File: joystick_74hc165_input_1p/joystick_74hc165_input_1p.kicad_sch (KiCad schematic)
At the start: 11 parts, among them J1 Conn_01x18_Male

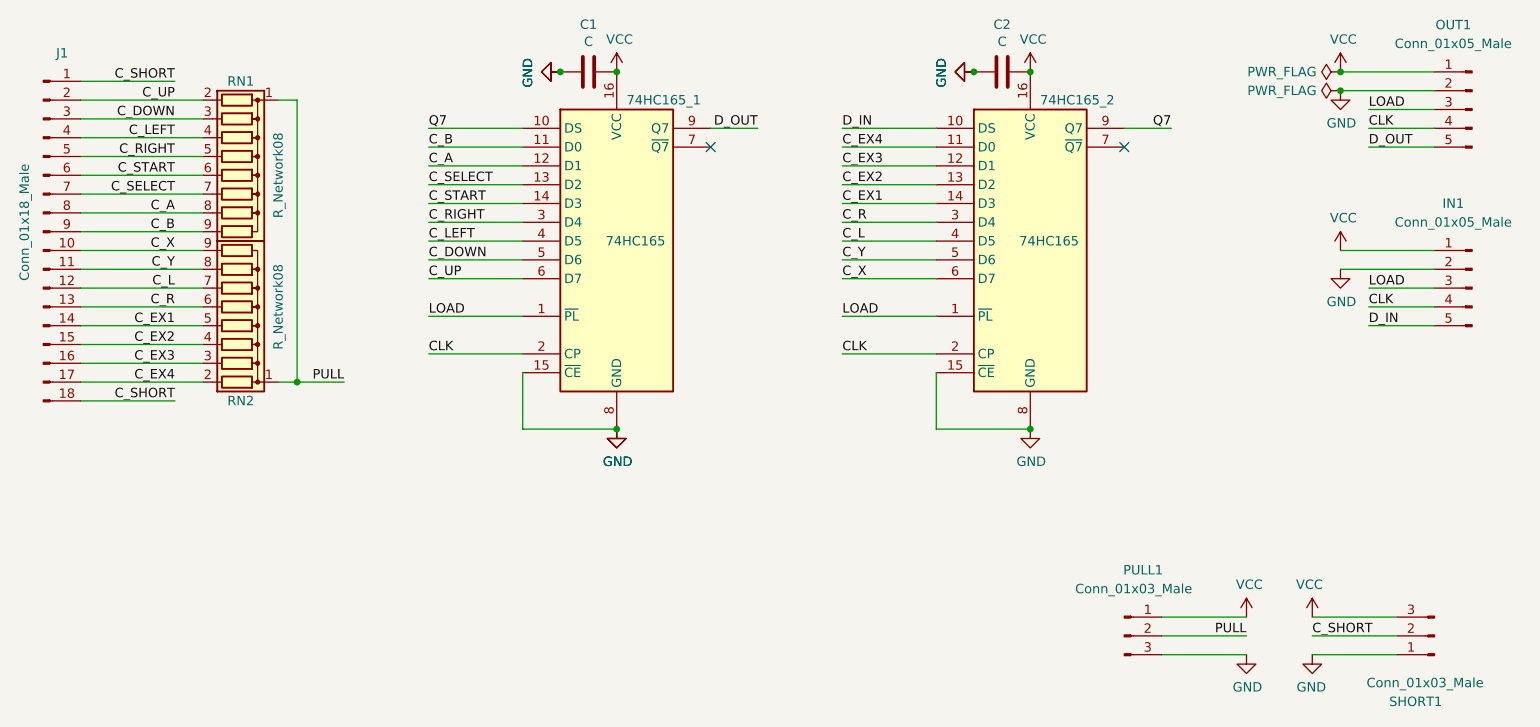
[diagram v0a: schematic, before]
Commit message: 부품 값 입력
Signed-off-by: Ju, Gyeong-min <jcmh74@gmail.com>
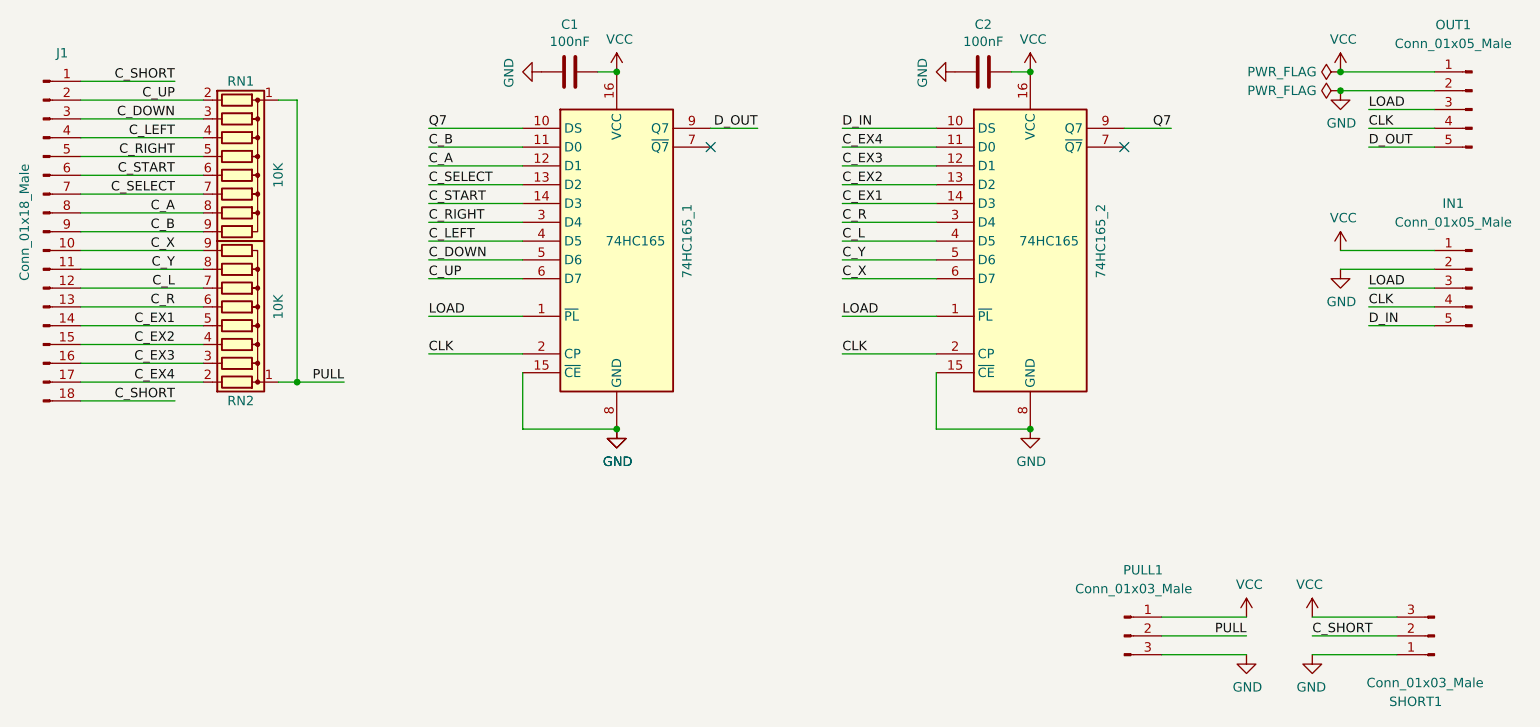
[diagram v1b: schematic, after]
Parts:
- C1, C2: value C -> 100nF
- RN1, RN2: value R_Network08 -> 10K
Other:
- moved on the sheet: C1, C2
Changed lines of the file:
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@@
   (junction (at 229.87 50.8) (diameter 0) (color 0 0 0 0)
   )
-  (junction (at 124.46 48.26) (diameter 0) (color 0 0 0 0)
-  )
   (junction (at 88.9 90.17) (diameter 0) (color 0 0 0 0)
   )
   (junction (at 132.08 96.52) (diameter 0) (color 0 0 0 0)
-  )
-  (junction (at 180.34 48.26) (diameter 0) (color 0 0 0 0)
   )
   (junction (at 132.08 48.26) (diameter 0) (color 0 0 0 0)
@@
     (stroke (width 0) (type default) (color 0 0 0 0))
   )
+  (wire (pts (xy 185.42 48.26) (xy 187.96 48.26))
+    (stroke (width 0) (type default) (color 0 0 0 0))
+  )
   (wire (pts (xy 151.13 55.88) (xy 144.78 55.88))
     (stroke (width 0) (type default) (color 0 0 0 0))
@@
     (stroke (width 0) (type default) (color 0 0 0 0))
   )
+  (wire (pts (xy 129.54 48.26) (xy 132.08 48.26))
+    (stroke (width 0) (type default) (color 0 0 0 0))
+  )
   (wire (pts (xy 59.69 67.31) (xy 76.2 67.31))
     (stroke (width 0) (type default) (color 0 0 0 0))
@@
   (symbol (lib_id "74xx:74HC165") (at 132.08 71.12 0) (unit 1)
     (in_bom yes) (on_board yes)
-    (property "Reference" "74HC165_1" (id 0) (at 138.43 52.07 0))
+    (property "Reference" "74HC165_1" (id 0) (at 141.605 71.12 90))
     (property "Value" "74HC165" (id 1) (at 134.62 71.12 0))
     (property "Footprint" "Package_DIP:DIP-16_W7.62mm" (id 2) (at 132.08 71.12 0)
@@
   (symbol (lib_id "74xx:74HC165") (at 187.96 71.12 0) (unit 1)
     (in_bom yes) (on_board yes)
-    (property "Reference" "74HC165_2" (id 0) (at 194.31 52.07 0))
+    (property "Reference" "74HC165_2" (id 0) (at 197.485 71.12 90))
     (property "Value" "74HC165" (id 1) (at 190.5 71.12 0))
     (property "Footprint" "Package_DIP:DIP-16_W7.62mm" (id 2) (at 187.96 71.12 0)
@@
     (in_bom yes) (on_board yes)
     (property "Reference" "RN2" (id 0) (at 81.28 92.71 90))
-    (property "Value" "R_Network08" (id 1) (at 86.36 80.01 0))
+    (property "Value" "10K" (id 1) (at 86.36 80.01 0))
     (property "Footprint" "Resistor_THT:R_Array_SIP9" (id 2) (at 81.28 67.945 90)
       (effects (font (size 1.27 1.27)) hide)
@@
     (in_bom yes) (on_board yes)
     (property "Reference" "RN1" (id 0) (at 81.28 49.53 90))
-    (property "Value" "R_Network08" (id 1) (at 86.36 62.23 0))
+    (property "Value" "10K" (id 1) (at 86.36 62.23 0))
     (property "Footprint" "Resistor_THT:R_Array_SIP9" (id 2) (at 81.28 74.295 90)
       (effects (font (size 1.27 1.27)) hide)
@@
     (pin "9")
   )
-  (symbol (lib_id "Device:C") (at 128.27 48.26 270) (unit 1)
-    (in_bom yes) (on_board yes)
-    (property "Reference" "C1" (id 0) (at 128.27 41.8592 90))
-    (property "Value" "C" (id 1) (at 128.27 44.1706 90))
-    (property "Footprint" "Capacitor_THT:C_Disc_D4.3mm_W1.9mm_P5.00mm" (id 2) (at 124.46 49.2252 0)
-      (effects (font (size 1.27 1.27)) hide)
-    )
-    (property "Datasheet" "~" (id 3) (at 128.27 48.26 0)
+  (symbol (lib_id "Device:C") (at 125.73 48.26 270) (unit 1)
+    (in_bom yes) (on_board yes)
+    (property "Reference" "C1" (id 0) (at 125.73 41.8592 90))
+    (property "Value" "100nF" (id 1) (at 125.73 44.1706 90))
+    (property "Footprint" "Capacitor_THT:C_Disc_D4.3mm_W1.9mm_P5.00mm" (id 2) (at 121.92 49.2252 0)
+      (effects (font (size 1.27 1.27)) hide)
+    )
+    (property "Datasheet" "~" (id 3) (at 125.73 48.26 0)
       (effects (font (size 1.27 1.27)) hide)
     )
@@
     (pin "1")
   )
-  (symbol (lib_id "power:GND") (at 124.46 48.26 270) (unit 1)
-    (in_bom yes) (on_board yes)
-    (property "Reference" "#PWR01" (id 0) (at 118.11 48.26 0)
-      (effects (font (size 1.27 1.27)) hide)
-    )
-    (property "Value" "GND" (id 1) (at 120.0658 48.387 0))
-    (property "Footprint" "" (id 2) (at 124.46 48.26 0)
-      (effects (font (size 1.27 1.27)) hide)
-    )
-    (property "Datasheet" "" (id 3) (at 124.46 48.26 0)
-      (effects (font (size 1.27 1.27)) hide)
-    )
-    (pin "1")
-  )
-  (symbol (lib_id "power:GND") (at 124.46 48.26 270) (unit 1)
-    (in_bom yes) (on_board yes)
-    (property "Reference" "#PWR02" (id 0) (at 118.11 48.26 0)
-      (effects (font (size 1.27 1.27)) hide)
-    )
-    (property "Value" "GND" (id 1) (at 120.0658 48.387 0))
-    (property "Footprint" "" (id 2) (at 124.46 48.26 0)
-      (effects (font (size 1.27 1.27)) hide)
-    )
-    (property "Datasheet" "" (id 3) (at 124.46 48.26 0)
-      (effects (font (size 1.27 1.27)) hide)
-    )
-    (pin "1")
-  )
-  (symbol (lib_id "Device:C") (at 184.15 48.26 270) (unit 1)
-    (in_bom yes) (on_board yes)
-    (property "Reference" "C2" (id 0) (at 184.15 41.8592 90))
-    (property "Value" "C" (id 1) (at 184.15 44.1706 90))
-    (property "Footprint" "Capacitor_THT:C_Disc_D4.3mm_W1.9mm_P5.00mm" (id 2) (at 180.34 49.2252 0)
-      (effects (font (size 1.27 1.27)) hide)
-    )
-    (property "Datasheet" "~" (id 3) (at 184.15 48.26 0)
-      (effects (font (size 1.27 1.27)) hide)
-    )
-    (pin "1")
-    (pin "2")
-  )
-  (symbol (lib_id "power:GND") (at 180.34 48.26 270) (unit 1)
-    (in_bom yes) (on_board yes)
-    (property "Reference" "#PWR04" (id 0) (at 173.99 48.26 0)
-      (effects (font (size 1.27 1.27)) hide)
-    )
-    (property "Value" "GND" (id 1) (at 175.9458 48.387 0))
-    (property "Footprint" "" (id 2) (at 180.34 48.26 0)
-      (effects (font (size 1.27 1.27)) hide)
-    )
-    (property "Datasheet" "" (id 3) (at 180.34 48.26 0)
-      (effects (font (size 1.27 1.27)) hide)
-    )
-    (pin "1")
-  )
-  (symbol (lib_id "power:GND") (at 180.34 48.26 270) (unit 1)
-    (in_bom yes) (on_board yes)
-    (property "Reference" "#PWR05" (id 0) (at 173.99 48.26 0)
-      (effects (font (size 1.27 1.27)) hide)
-    )
-    (property "Value" "GND" (id 1) (at 175.9458 48.387 0))
-    (property "Footprint" "" (id 2) (at 180.34 48.26 0)
-      (effects (font (size 1.27 1.27)) hide)
-    )
-    (property "Datasheet" "" (id 3) (at 180.34 48.26 0)
+  (symbol (lib_id "power:GND") (at 121.92 48.26 270) (unit 1)
+    (in_bom yes) (on_board yes)
+    (property "Reference" "#PWR01" (id 0) (at 115.57 48.26 0)
+      (effects (font (size 1.27 1.27)) hide)
+    )
+    (property "Value" "GND" (id 1) (at 117.5258 48.387 0))
+    (property "Footprint" "" (id 2) (at 121.92 48.26 0)
+      (effects (font (size 1.27 1.27)) hide)
+    )
+    (property "Datasheet" "" (id 3) (at 121.92 48.26 0)
+      (effects (font (size 1.27 1.27)) hide)
+    )
+    (pin "1")
+  )
+  (symbol (lib_id "Device:C") (at 181.61 48.26 270) (unit 1)
+    (in_bom yes) (on_board yes)
+    (property "Reference" "C2" (id 0) (at 181.61 41.8592 90))
+    (property "Value" "100nF" (id 1) (at 181.61 44.1706 90))
+    (property "Footprint" "Capacitor_THT:C_Disc_D4.3mm_W1.9mm_P5.00mm" (id 2) (at 177.8 49.2252 0)
+      (effects (font (size 1.27 1.27)) hide)
+    )
+    (property "Datasheet" "~" (id 3) (at 181.61 48.26 0)
+      (effects (font (size 1.27 1.27)) hide)
+    )
+    (pin "1")
+    (pin "2")
+  )
+  (symbol (lib_id "power:GND") (at 177.8 48.26 270) (unit 1)
+    (in_bom yes) (on_board yes)
+    (property "Reference" "#PWR05" (id 0) (at 171.45 48.26 0)
+      (effects (font (size 1.27 1.27)) hide)
+    )
+    (property "Value" "GND" (id 1) (at 173.4058 48.387 0))
+    (property "Footprint" "" (id 2) (at 177.8 48.26 0)
+      (effects (font (size 1.27 1.27)) hide)
+    )
+    (property "Datasheet" "" (id 3) (at 177.8 48.26 0)
       (effects (font (size 1.27 1.27)) hide)
     )
@@
       (reference "#PWR01") (unit 1) (value "GND") (footprint "")
     )
-    (path "/00000000-0000-0000-0000-0000617090f5"
-      (reference "#PWR02") (unit 1) (value "GND") (footprint "")
-    )
     (path "/00000000-0000-0000-0000-00006170839c"
       (reference "#PWR03") (unit 1) (value "GND") (footprint "")
     )
-    (path "/00000000-0000-0000-0000-00006170c627"
-      (reference "#PWR04") (unit 1) (value "GND") (footprint "")
-    )
     (path "/00000000-0000-0000-0000-00006170c62d"
       (reference "#PWR05") (unit 1) (value "GND") (footprint "")
@@
     )
     (path "/00000000-0000-0000-0000-000061706598"
-      (reference "C1") (unit 1) (value "C") (footprint "Capacitor_THT:C_Disc_D4.3mm_W1.9mm_P5.00mm")
+      (reference "C1") (unit 1) (value "100nF") (footprint "Capacitor_THT:C_Disc_D4.3mm_W1.9mm_P5.00mm")
     )
     (path "/00000000-0000-0000-0000-00006170c621"
-      (reference "C2") (unit 1) (value "C") (footprint "Capacitor_THT:C_Disc_D4.3mm_W1.9mm_P5.00mm")
+      (reference "C2") (unit 1) (value "100nF") (footprint "Capacitor_THT:C_Disc_D4.3mm_W1.9mm_P5.00mm")
     )
     (path "/00000000-0000-0000-0000-00006135617b"
@@
     )
     (path "/00000000-0000-0000-0000-000061516673"
-      (reference "RN1") (unit 1) (value "R_Network08") (footprint "Resistor_THT:R_Array_SIP9")
+      (reference "RN1") (unit 1) (value "10K") (footprint "Resistor_THT:R_Array_SIP9")
     )
     (path "/00000000-0000-0000-0000-0000614b9f97"
-      (reference "RN2") (unit 1) (value "R_Network08") (footprint "Resistor_THT:R_Array_SIP9")
+      (reference "RN2") (unit 1) (value "10K") (footprint "Resistor_THT:R_Array_SIP9")
     )
     (path "/00000000-0000-0000-0000-0000613769c0"
